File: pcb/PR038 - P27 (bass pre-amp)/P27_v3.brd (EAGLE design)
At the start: 41.9 x 64.8 mm, 51 parts, among them IC1 NE5532P, Q1 BC337

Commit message: 
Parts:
- C13, C14, C15, C16: value (none) -> 220uF/25V
- D5, D6, D7, D8: value 1N4004D -> 1N4007
- IC2: value (none) -> 7815
- IC3: value (none) -> 7915
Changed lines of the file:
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@@
 <?xml version="1.0" encoding="utf-8"?>
 <!DOCTYPE eagle SYSTEM "eagle.dtd">
-<eagle version="6.4">
+<eagle version="6.5.0">
 <drawing>
 <settings>
@@
 <element name="BRIGHT" library="P27" package="1X02" value="" x="15.24" y="5.08" rot="R180"/>
 <element name="X1" library="P27" package="W237-103" value="" x="8.89" y="33.655" rot="R270"/>
-<element name="IC2" library="P27" package="78XXS" value="" x="5.715" y="48.26" rot="R90"/>
-<element name="C13" library="P27" package="E2,5-6" value="" x="13.97" y="51.435" rot="R90"/>
-<element name="C14" library="P27" package="E2,5-6" value="" x="13.335" y="22.225" rot="R270"/>
-<element name="C15" library="P27" package="E2,5-6" value="" x="13.335" y="15.875" rot="R270"/>
-<element name="C16" library="P27" package="E2,5-6" value="" x="13.97" y="45.085" rot="R90"/>
-<element name="IC3" library="P27" package="79XXS" value="" x="5.715" y="19.05" rot="R90"/>
+<element name="IC2" library="P27" package="78XXS" value="7815" x="5.715" y="48.26" rot="R90"/>
+<element name="C13" library="P27" package="E2,5-6" value="220uF/25V" x="13.97" y="51.435" rot="R90"/>
+<element name="C14" library="P27" package="E2,5-6" value="220uF/25V" x="13.335" y="22.225" rot="R270"/>
+<element name="C15" library="P27" package="E2,5-6" value="220uF/25V" x="13.335" y="15.875" rot="R270"/>
+<element name="C16" library="P27" package="E2,5-6" value="220uF/25V" x="13.97" y="45.085" rot="R90"/>
+<element name="IC3" library="P27" package="79XXS" value="7915" x="5.715" y="19.05" rot="R90"/>
 <element name="Q1" library="P27" package="TO92" value="BC337" x="38.1" y="33.655" rot="R270"/>
-<element name="D5" library="P27" package="DO41-7" value="1N4004D" x="16.51" y="37.465" rot="R180"/>
-<element name="D6" library="P27" package="DO41-7" value="1N4004D" x="16.51" y="34.925" rot="R180"/>
-<element name="D7" library="P27" package="DO41-7" value="1N4004D" x="16.51" y="29.845"/>
-<element name="D8" library="P27" package="DO41-7" value="1N4004D" x="16.51" y="32.385"/>
+<element name="D5" library="P27" package="DO41-7" value="1N4007" x="16.51" y="37.465" rot="R180"/>
+<element name="D6" library="P27" package="DO41-7" value="1N4007" x="16.51" y="34.925" rot="R180"/>
+<element name="D7" library="P27" package="DO41-7" value="1N4007" x="16.51" y="29.845"/>
+<element name="D8" library="P27" package="DO41-7" value="1N4007" x="16.51" y="32.385"/>
 </elements>
 <signals>

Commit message: 
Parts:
- D1, D2, D3, D4: value 1N4004D -> 1N4148
- Q1: value BC337 -> BC549
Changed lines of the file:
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@@
 <element name="R12" library="P27" package="0207/7" value="4k7" x="31.75" y="54.61" rot="R270"/>
 <element name="R13" library="P27" package="0207/7" value="220" x="34.29" y="54.61" rot="R90"/>
-<element name="D1" library="P27" package="DO41-7" value="1N4004D" x="36.83" y="44.45" rot="R90"/>
-<element name="D2" library="P27" package="DO41-7" value="1N4004D" x="36.83" y="54.61" rot="R90"/>
-<element name="D3" library="P27" package="DO41-7" value="1N4004D" x="39.37" y="44.45" rot="R270"/>
-<element name="D4" library="P27" package="DO41-7" value="1N4004D" x="39.37" y="54.61" rot="R270"/>
+<element name="D1" library="P27" package="DO41-7" value="1N4148" x="36.83" y="44.45" rot="R90"/>
+<element name="D2" library="P27" package="DO41-7" value="1N4148" x="36.83" y="54.61" rot="R90"/>
+<element name="D3" library="P27" package="DO41-7" value="1N4148" x="39.37" y="44.45" rot="R270"/>
+<element name="D4" library="P27" package="DO41-7" value="1N4148" x="39.37" y="54.61" rot="R270"/>
 <element name="MASTER" library="P27" package="1X02" value="" x="33.02" y="62.23" rot="R180"/>
 <element name="C10" library="P27" package="C050-025X075" value="2.2uF" x="39.37" y="22.86" rot="R270"/>
@@
 <element name="C16" library="P27" package="E2,5-6" value="220uF/25V" x="13.97" y="45.085" rot="R90"/>
 <element name="IC3" library="P27" package="79XXS" value="7915" x="5.715" y="19.05" rot="R90"/>
-<element name="Q1" library="P27" package="TO92" value="BC337" x="38.1" y="33.655" rot="R270"/>
+<element name="Q1" library="P27" package="TO92" value="BC549" x="38.1" y="33.655" rot="R270"/>
 <element name="D5" library="P27" package="DO41-7" value="1N4007" x="16.51" y="37.465" rot="R180"/>
 <element name="D6" library="P27" package="DO41-7" value="1N4007" x="16.51" y="34.925" rot="R180"/>

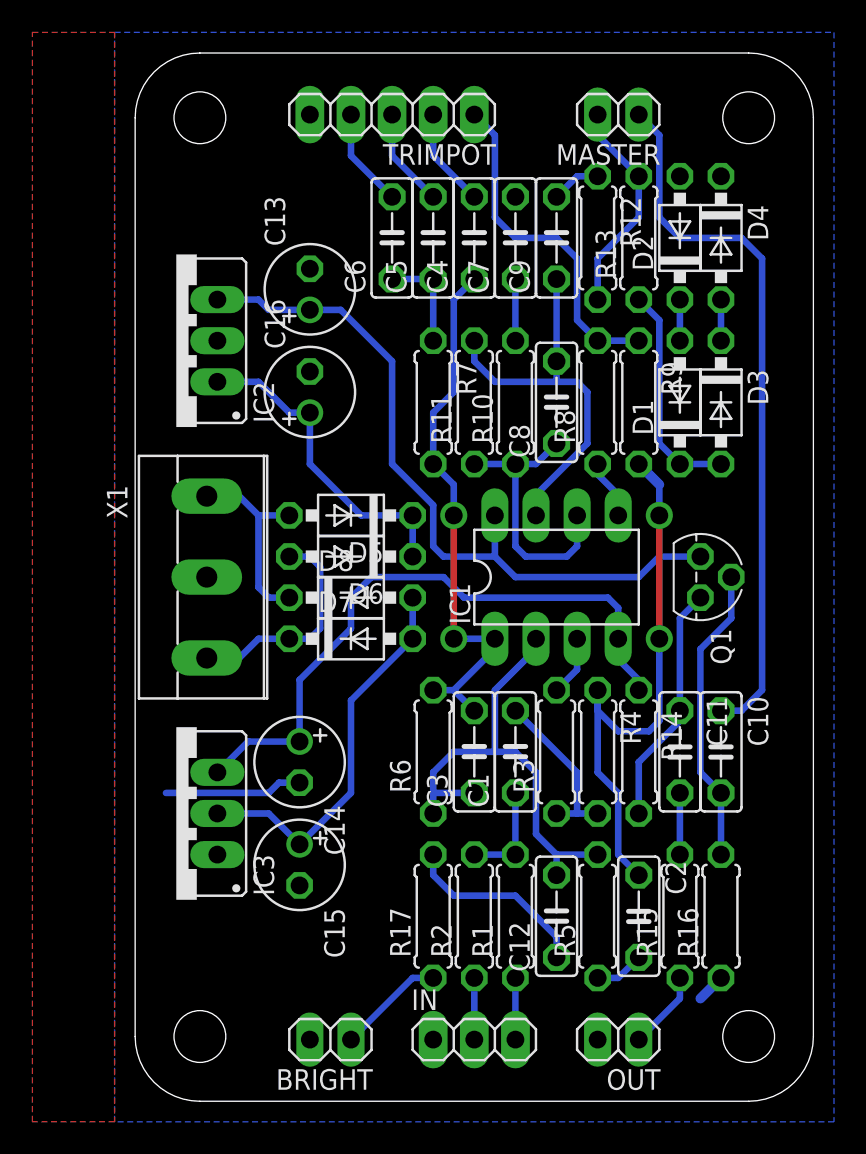
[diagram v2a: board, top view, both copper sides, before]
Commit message: 
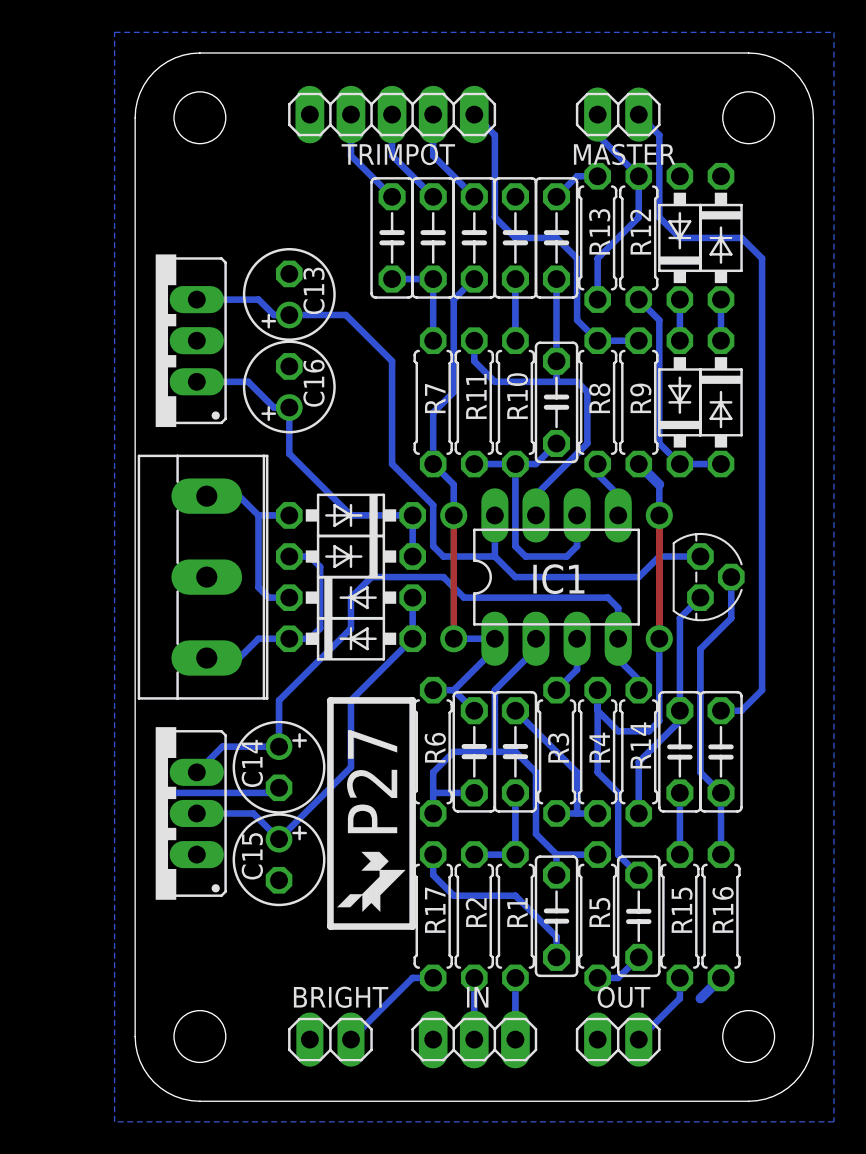
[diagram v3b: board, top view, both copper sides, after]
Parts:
- added U$1: (no value), P27:FOX-1
- moved C13 1.31 mm to (12.7, 51.1)
- moved C14 1.31 mm to (12.1, 21.9)
- moved C16 1.31 mm to (12.7, 45.4)
- moved C15 1.31 mm to (12.1, 16.2)
- moved IC2 1.27 mm to (4.45, 48.3)
- moved IC3 1.27 mm to (4.45, 19.1)
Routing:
- net +12V: track 45.9 -> 47.1 mm
- net N$32: track 19.9 -> 21.0 mm
- net AGND: track 45.1 -> 44.1 mm
- net -12V: track 39.5 -> 40.2 mm
- removed copper zone on layer 1, net AGND
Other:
- board text added: "P27"
